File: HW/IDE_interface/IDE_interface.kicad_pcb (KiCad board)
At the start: 2 copper layers, 149.9 x 88.9 mm, 16 parts, among them P1 EXPANSION PORT, P2 IDE0, U1 74LS32, U2 74LS139, U3 74HC74, U4 74LS08, U5 DS1511Y+, U6 74LS574, U7 74LS574, U8 74HC245

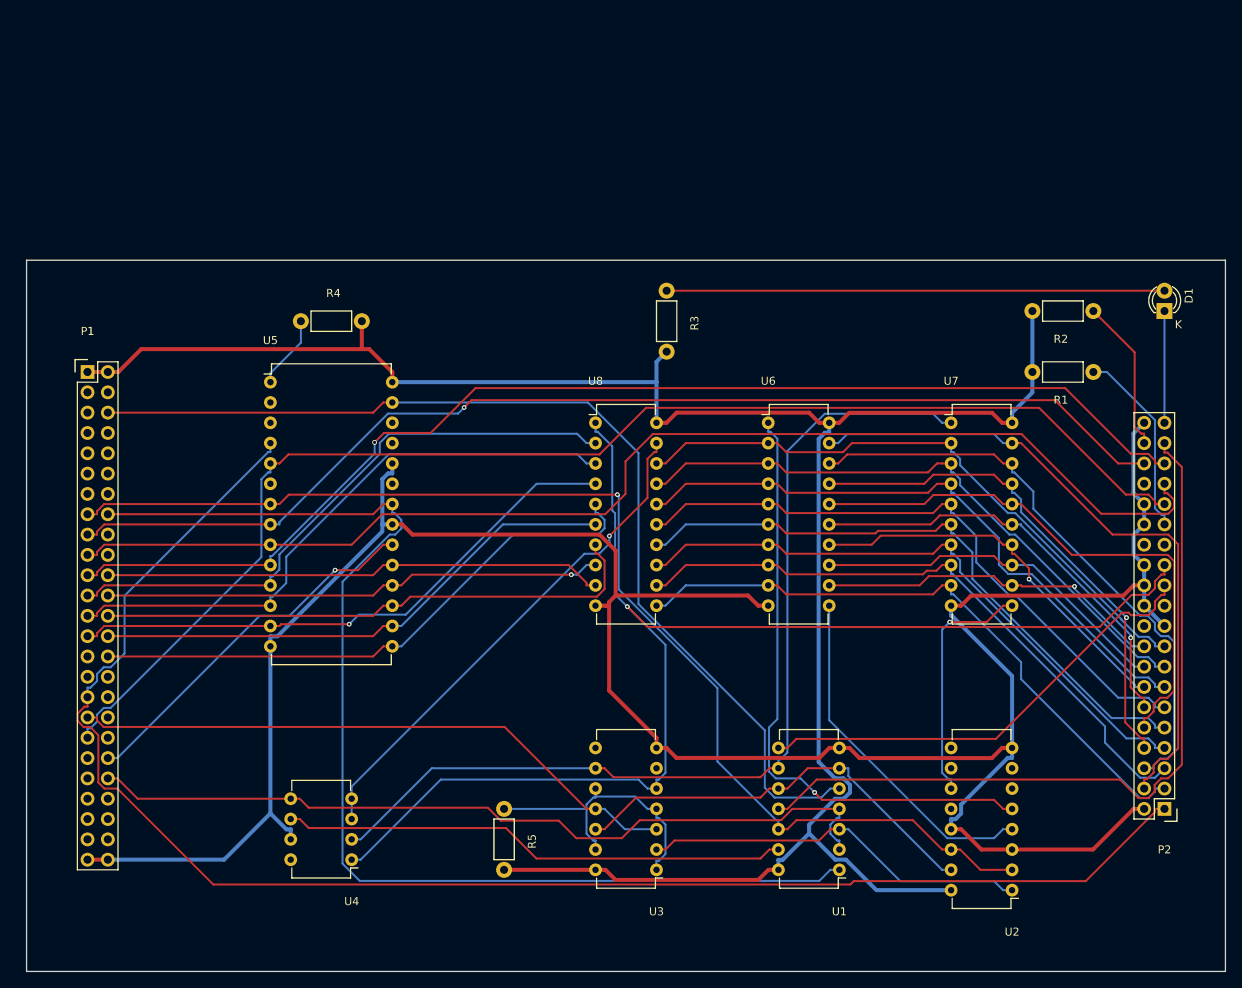
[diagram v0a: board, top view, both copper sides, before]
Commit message: New MB design. Includes RTC. New IDE design.
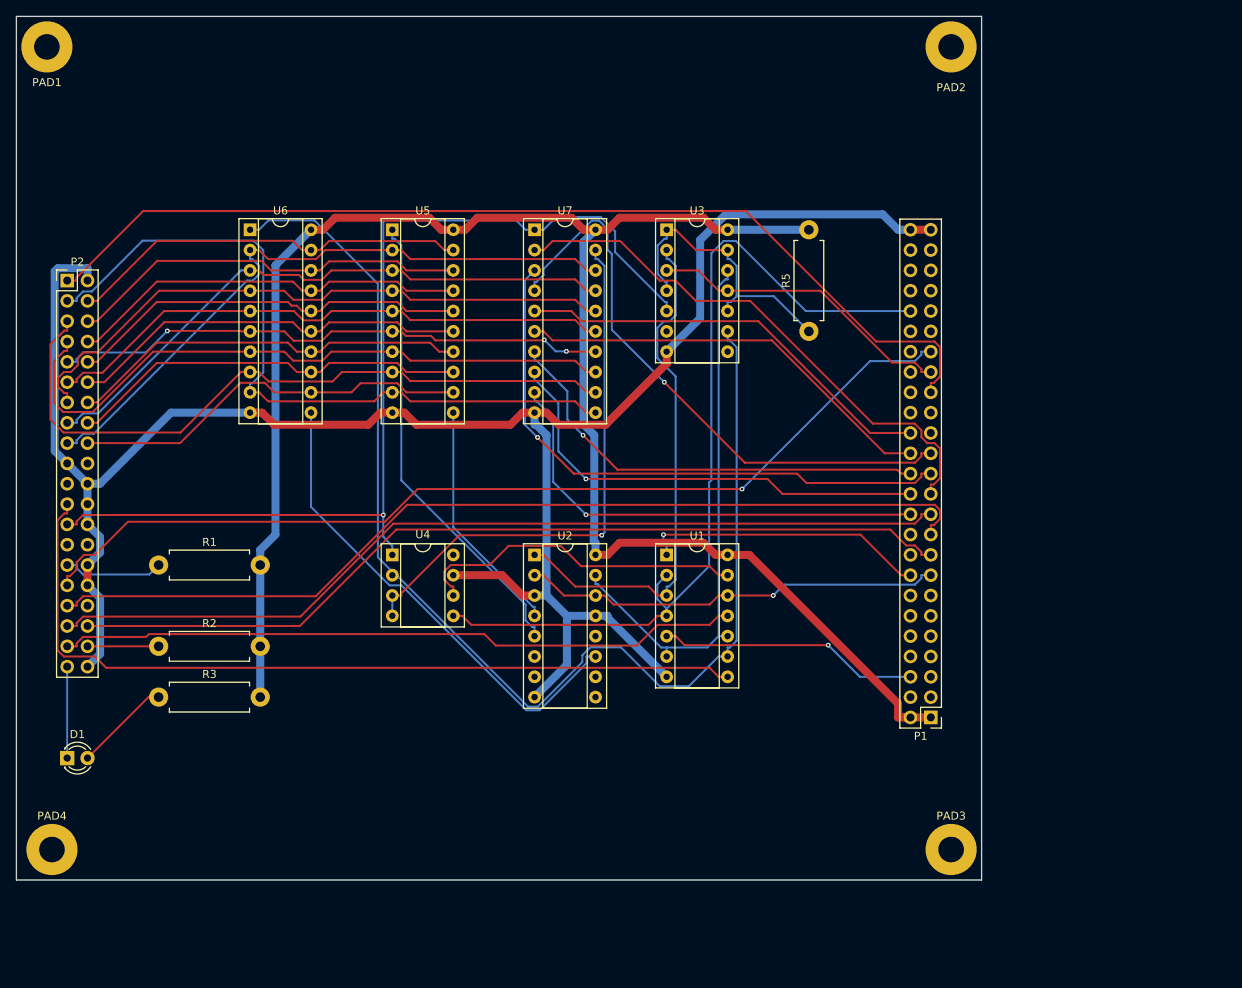
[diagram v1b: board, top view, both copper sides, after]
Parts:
- removed R4: 3.3K, Resistors_ThroughHole:Resistor_Horizontal_RM7mm
- removed U8: 74HC245, Housings_DIP:DIP-20_W7.62mm
- added PAD1: MountingHole_3.2mm_M3_Pad, Mounting_Holes:MountingHole_3.2mm_M3_Pad, F.Cu at (52.1, 45.7)
- added PAD2: MountingHole_3.2mm_M3_Pad, Mounting_Holes:MountingHole_3.2mm_M3_Pad, F.Cu at (165.1, 45.7)
- added PAD3: MountingHole_3.2mm_M3_Pad, Mounting_Holes:MountingHole_3.2mm_M3_Pad, F.Cu at (165.1, 146.1)
- added PAD4: MountingHole_3.2mm_M3_Pad, Mounting_Holes:MountingHole_3.2mm_M3_Pad, F.Cu at (52.7, 146.1)
- D1: footprint LEDs:LED-3MM -> LEDs:LED_D3.0mm
- P1: footprint Pin_Headers:Pin_Header_Straight_2x25 -> Pin_Headers:Pin_Header_Straight_2x25_Pitch2.54mm
- P2: footprint Pin_Headers:Pin_Header_Straight_2x20 -> Pin_Headers:Pin_Header_Straight_2x20_Pitch2.54mm
- R1, R2, R3, R5: footprint Resistors_ThroughHole:Resistor_Horizontal_RM7mm -> Resistors_ThroughHole:R_Axial_DIN0411_L9.9mm_D3.6mm_P12.70mm_Horizontal
- U1, U3: footprint Housings_DIP:DIP-14_W7.62mm -> Housings_DIP:DIP-14_W7.62mm_Socket
- U2: footprint Housings_DIP:DIP-16_W7.62mm -> Housings_DIP:DIP-16_W7.62mm_Socket
- U4: footprint Housings_DIP:DIP-8_W7.62mm -> Housings_DIP:DIP-8_W7.62mm_Socket
- U5: value DS1511Y+ -> 74LS574; footprint Housings_DIP:DIP-28_W15.24mm -> Housings_DIP:DIP-20_W7.62mm_Socket
- U6: footprint Housings_DIP:DIP-20_W7.62mm -> Housings_DIP:DIP-20_W7.62mm_Socket
- U7: value 74LS574 -> 74HC245; footprint Housings_DIP:DIP-20_W7.62mm -> Housings_DIP:DIP-20_W7.62mm_Socket
- moved P2 152.2 mm to (54.6, 74.9), turned to 0 degrees
- moved D1 148.1 mm to (54.6, 134.6), turned to 0 degrees
- moved R2 124.1 mm to (66.0, 120.7), turned to 0 degrees
- moved R1 119.3 mm to (66.0, 110.5), turned to 0 degrees
- moved P1 113.9 mm to (162.6, 129.5), turned to 180 degrees
- moved R3 81.3 mm to (66.0, 127.0), turned to 0 degrees
- moved U3 80.0 mm to (129.5, 68.6), turned to 0 degrees
- moved U2 72.9 mm to (113.0, 109.2), turned to 0 degrees
- moved R5 70.8 mm to (147.3, 81.3), turned to 90 degrees
- moved U6 69.1 mm to (77.5, 68.6)
- moved U7 57.4 mm to (113.0, 68.6)
- moved U1 44.9 mm to (129.5, 109.2), turned to 0 degrees
- moved U4 38.4 mm to (95.2, 109.2), turned to 0 degrees
- moved U5 24.4 mm to (95.2, 68.6)
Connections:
- net /~7F4X renamed /~7F8X
- P1 pad 10: /A8 -> (no net)
- P1 pad 11: /A5 -> (no net)
- P1 pad 12: /A9 -> (no net)
- P1 pad 13: /A4 -> (no net)
- P1 pad 14: /A11 -> (no net)
- P1 pad 18: /A10 -> (no net)
- P1 pad 20: Net-(P1-Pad20) -> (no net)
- P1 pad 29: Net-(P1-Pad29) -> (no net)
- P1 pad 3: /A14 -> (no net)
- P1 pad 31: Net-(P1-Pad31) -> (no net)
- P1 pad 32: /A15 -> (no net)
- P1 pad 34: /~7F0X -> (no net)
- P1 pad 36: /~7F1X -> (no net)
- P1 pad 38: /~7F2X -> (no net)
- P1 pad 39: /~7FXX -> (no net)
- P1 pad 4: Net-(P1-Pad4) -> (no net)
- P1 pad 40: /~7F3X -> (no net)
- P1 pad 41: /~NMI -> (no net)
- P1 pad 43: /~R/W -> (no net)
- P1 pad 44: /~7F5X -> (no net)
- P1 pad 45: Net-(P1-Pad45) -> (no net)
- P1 pad 46: /~7F6X -> (no net)
- P1 pad 47: Net-(P1-Pad47) -> (no net)
- P1 pad 48: /~7F7X -> (no net)
- P1 pad 5: /A12 -> (no net)
- P1 pad 7: /A7 -> (no net)
- P1 pad 8: /A13 -> (no net)
- P1 pad 9: /A6 -> (no net)
- P2 pad 20: Net-(P2-Pad20) -> (no net)
- P2 pad 21: /DMARQ -> (no net)
- P2 pad 27: /IORDY -> (no net)
- P2 pad 28: Net-(P2-Pad28) -> (no net)
- P2 pad 34: Net-(P2-Pad34) -> (no net)
- U2 pad 10: Net-(U2-Pad10) -> (no net)
- U2 pad 12: Net-(U2-Pad12) -> (no net)
- U2 pad 6: Net-(U2-Pad6) -> (no net)
- U2 pad 7: Net-(U2-Pad7) -> (no net)
- U2 pad 9: Net-(U2-Pad9) -> (no net)
- U3 pad 6: Net-(U3-Pad6) -> (no net)
- U3 pad 8: Net-(U3-Pad8) -> (no net)
- U5 pad 1: /~PWR -> Net-(U2-Pad5)
- U5 pad 10: /A0 -> GND
- U5 pad 11: /D0 -> Net-(U2-Pad4)
- U5 pad 12: /D1 -> /IDE-D15
- U5 pad 13: /D2 -> /IDE-D14
- U5 pad 14: GND -> /IDE-D13
- U5 pad 15: /D3 -> /IDE-D12
- U5 pad 16: /D4 -> /IDE-D11
- U5 pad 17: /D5 -> /IDE-D10
- U5 pad 18: /D6 -> /IDE-D9
- U5 pad 19: /D7 -> /IDE-D8
- U5 pad 2: (no net) -> /IDE-D0
- U5 pad 20: /~7F3X -> VCC
- U5 pad 3: (no net) -> /IDE-D1
- U5 pad 4: /~RES -> /IDE-D2
- U5 pad 5: /~IRQ -> /IDE-D3
- U5 pad 6: Net-(U5-Pad6) -> /IDE-D4
- U5 pad 7: /A3 -> /IDE-D5
- U5 pad 8: /A2 -> /IDE-D6
- U5 pad 9: /A1 -> /IDE-D7
- U6 pad 1: Net-(U2-Pad5) -> Net-(U1-Pad9)
- U6 pad 11: Net-(U2-Pad4) -> Net-(U2-Pad11)
- U7 pad 1: Net-(U1-Pad9) -> /~DIOR
- U7 pad 11: Net-(U2-Pad11) -> /IDE-D7
- U7 pad 12: /IDE-D15 -> /IDE-D6
- U7 pad 13: /IDE-D14 -> /IDE-D5
- U7 pad 14: /IDE-D13 -> /IDE-D4
- U7 pad 15: /IDE-D12 -> /IDE-D3
- U7 pad 16: /IDE-D11 -> /IDE-D2
- U7 pad 17: /IDE-D10 -> /IDE-D1
- U7 pad 18: /IDE-D9 -> /IDE-D0
- U7 pad 19: /IDE-D8 -> Net-(U4-Pad3)
- U7 pad 2: /IDE-D0 -> /D0
- U7 pad 3: /IDE-D1 -> /D1
- U7 pad 4: /IDE-D2 -> /D2
- U7 pad 5: /IDE-D3 -> /D3
- U7 pad 6: /IDE-D4 -> /D4
- U7 pad 7: /IDE-D5 -> /D5
- U7 pad 8: /IDE-D6 -> /D6
- U7 pad 9: /IDE-D7 -> /D7
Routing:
- net /~MRD: track 148.7 -> 35.7 mm, vias 0 -> 1
- net /A3: track 150.0 -> 52.8 mm
- net /~MWR: track 128.1 -> 32.6 mm, vias 0 -> 1
- net /~RES: track 197.7 -> 126.3 mm
- net GND: track 322.6 -> 257.6 mm
- net Net-(D1-Pad2): track 62.2 -> 12.0 mm
- net VCC: track 268.9 -> 221.6 mm
- net /~7F3X: track 46.6 -> 0.00 mm, vias 1 -> 0
- net /~DIOW: track 58.2 -> 104.1 mm
- net /~IRQ: track 164.5 -> 121.5 mm, vias 0 -> 1
- net /~DIOR: track 165.5 -> 126.0 mm
- net /CLK2: track 77.1 -> 38.5 mm
- net /A0: track 150.1 -> 114.2 mm, vias 1 -> 0
- net /A1: track 152.8 -> 118.6 mm
- net Net-(U1-Pad9): track 121.1 -> 154.9 mm
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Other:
- board size 149.9 x 88.9 mm -> 120.7 x 108 mm

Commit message: Updates to pcb and monitor.
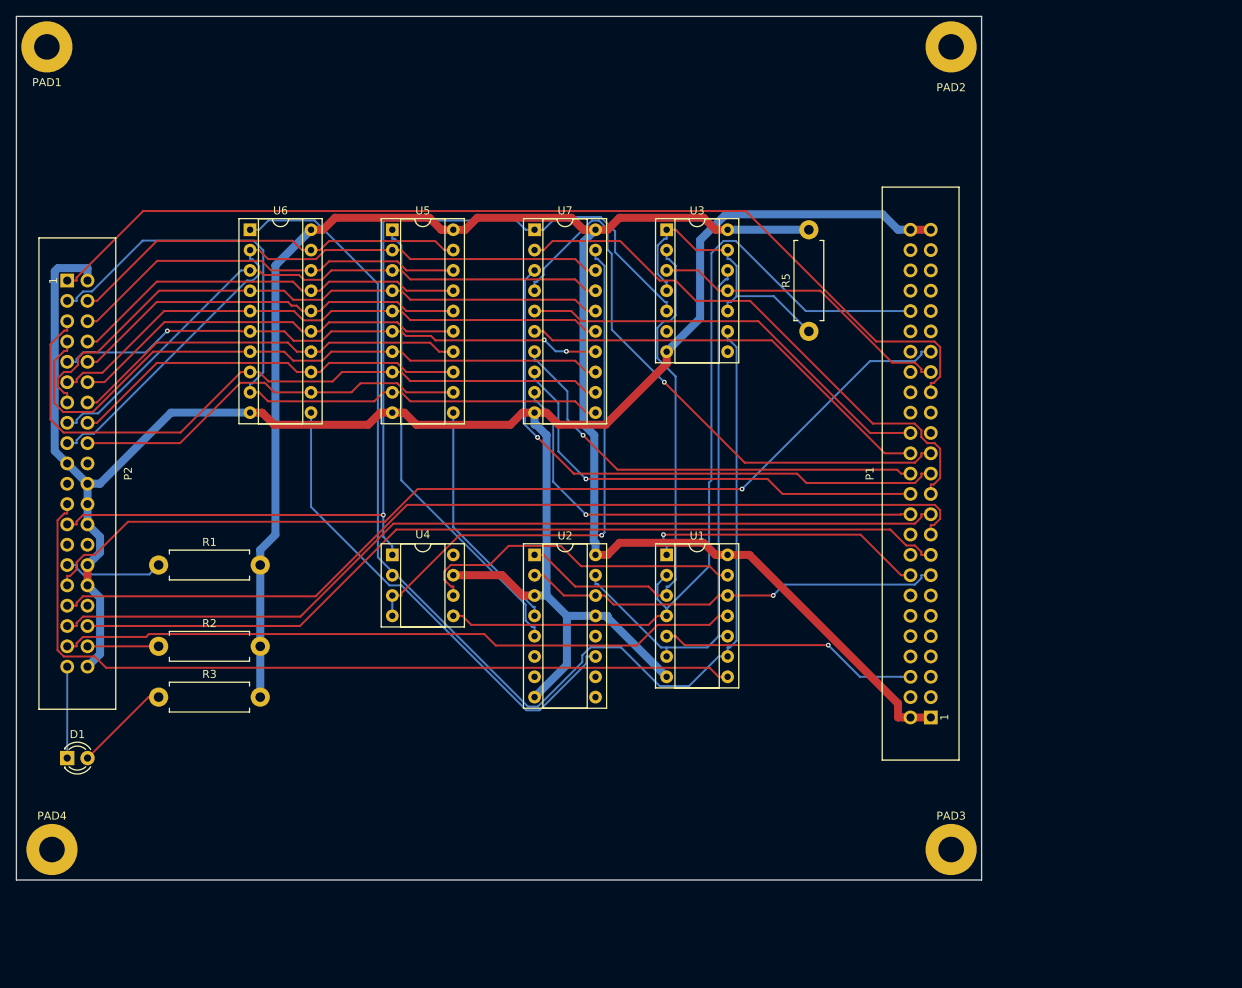
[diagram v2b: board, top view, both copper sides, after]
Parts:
- P1: footprint Pin_Headers:Pin_Header_Straight_2x25_Pitch2.54mm -> Connect:IDC_Header_Straight_50pins
- P2: footprint Pin_Headers:Pin_Header_Straight_2x20_Pitch2.54mm -> Connect:IDC_Header_Straight_40pins
- turned P1 to 90 degrees
- turned P2 to 270 degrees
